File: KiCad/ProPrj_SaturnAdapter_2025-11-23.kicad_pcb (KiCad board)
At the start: 2 copper layers, 51.5 x 41.2 mm, 32 parts

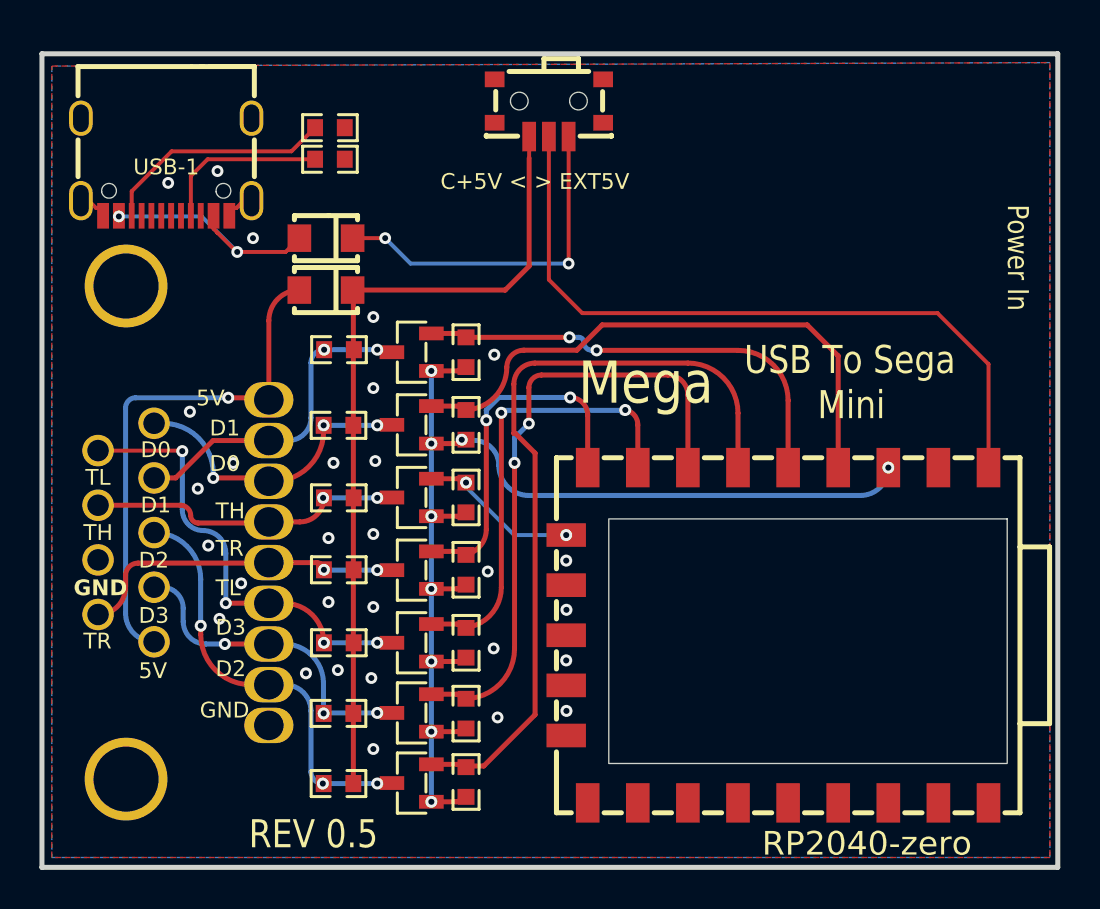
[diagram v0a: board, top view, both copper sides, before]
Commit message: Revert "Rev 0.5 changes | Moving of USB C port next to DB-9/MD connector"
This reverts commit 421da58faffa196843ed661754ba694fad0c3bff.
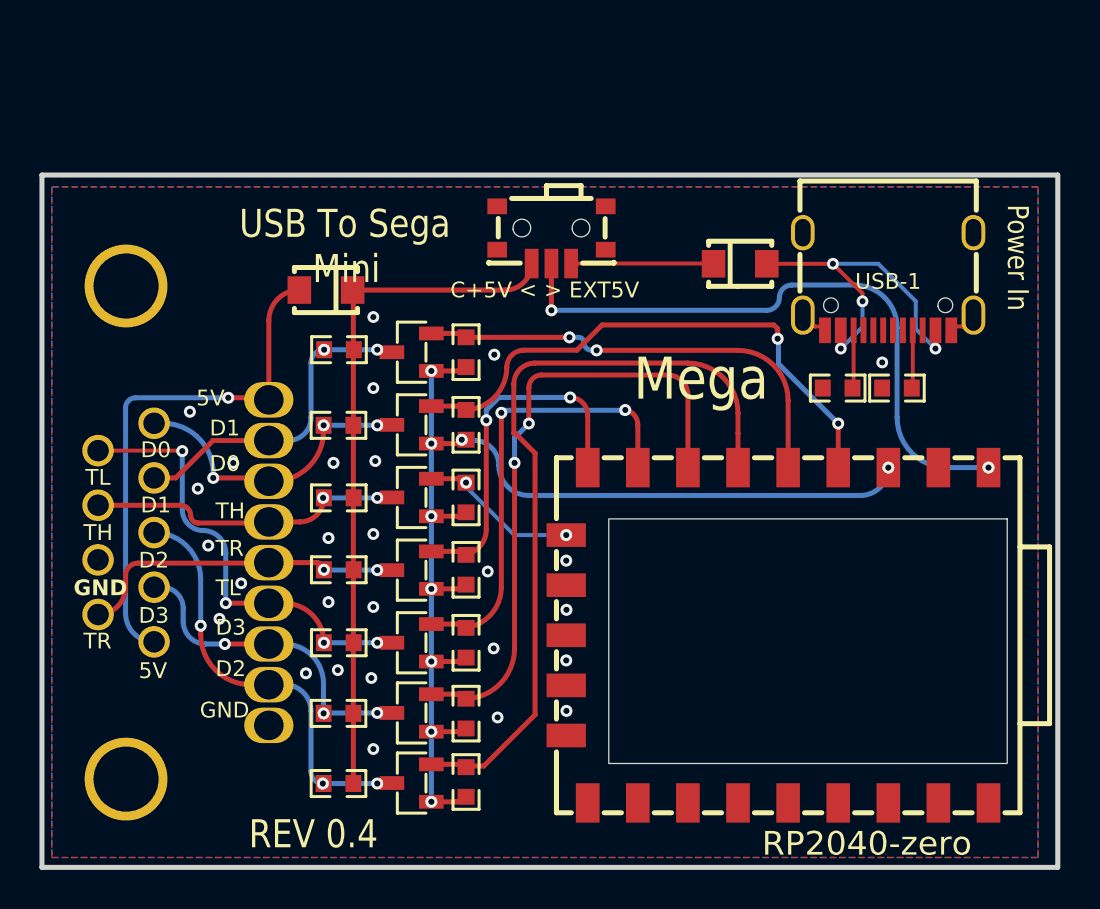
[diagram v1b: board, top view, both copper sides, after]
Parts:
- moved USB-1 37.1 mm to (165.4, 94.8)
- moved R16 31.0 mm to (165.8, 100.2), turned to 0 degrees
- moved R15 28.9 mm to (162.8, 100.2), turned to 0 degrees
- moved C2 21.0 mm to (157.9, 93.9), turned to 0 degrees
- moved SW1 6.44 mm to (148.3, 92.4)
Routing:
- net EXT5V: track 17.9 -> 7.23 mm, vias 2 -> 0
- net CC2: track 11.5 -> 2.95 mm
- net C+5V: track 41.1 -> 34.8 mm
- net OUT+5V: track 12.6 -> 18.5 mm, vias 2 -> 4
- net CC1: track 8.27 -> 2.99 mm
- net PICO+5V: track 36.6 -> 32.3 mm, vias 0 -> 2
- net LO_D0: track 29.2 -> 28.2 mm, vias 0 -> 2
- net GND: track 2.89 -> 2.72 mm, vias 29 -> 27
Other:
- board size 51.5 x 41.2 mm -> 51.5 x 35.1 mm
- board text added: "REV 0.4"
- board text removed: "REV 0.5"

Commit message: REV0.5 - Moved USB port next to controller port
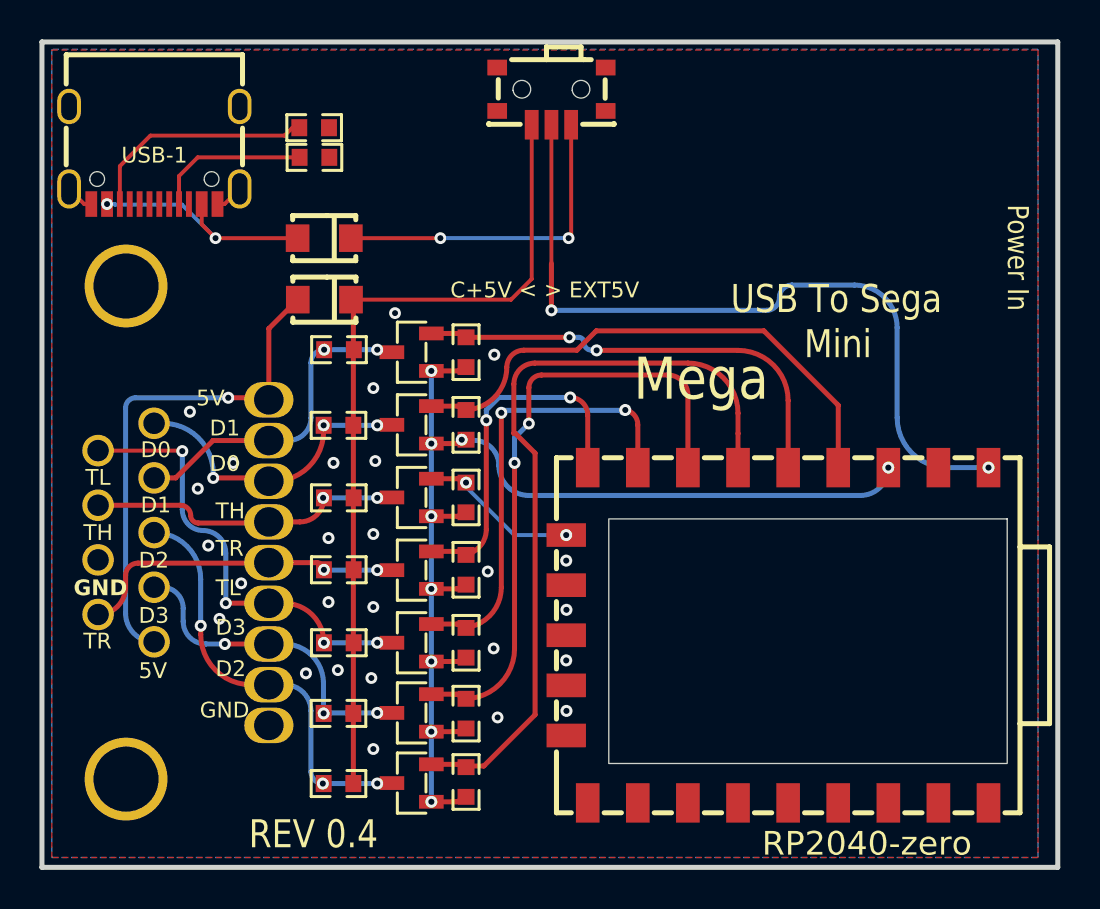
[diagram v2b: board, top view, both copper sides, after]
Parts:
- moved USB-1 37.7 mm to (128.2, 88.4)
- moved R16 31.8 mm to (136.3, 88.5), turned to 180 degrees
- moved R15 29.6 mm to (136.3, 87.0), turned to 180 degrees
- moved C2 21.1 mm to (136.8, 92.6), turned to 180 degrees
- moved SW1 7.04 mm to (148.3, 85.4)
- moved C1 0.49 mm to (136.8, 95.7)
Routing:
- net EXT5V: track 7.23 -> 16.8 mm, vias 0 -> 2
- net CC2: track 2.95 -> 11.8 mm
- net C+5V: track 34.8 -> 42.5 mm
- net PICO+5V: track 32.3 -> 39.3 mm
- net OUT+5V: track 18.5 -> 12.4 mm, vias 4 -> 2
- net CC1: track 2.99 -> 7.92 mm
- net LO_D0: track 28.2 -> 27.5 mm, vias 2 -> 0
- net IN+5V: track 26.6 -> 25.9 mm
- net GND: track 2.72 -> 2.89 mm, vias 27 -> 26
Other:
- board size 51.5 x 35.1 mm -> 51.5 x 41.8 mm
